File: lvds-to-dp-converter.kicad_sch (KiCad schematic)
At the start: 0 parts

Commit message: [#81876] Hierarchical design review fixes
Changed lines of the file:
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@@
 		(rev "1.0.0")
 	)
-	(hierarchical_label "PCIE_x4{PCIE}"
-		(shape bidirectional)
-		(at 123.19 99.06 0)
+	(hierarchical_label "DSI{DSI}"
+		(shape input)
+		(at 82.55 85.09 180)
 		(effects
 			(font
 				(size 1.27 1.27)
 			)
-			(justify left)
+			(justify right)
 		)
 	)
-	(hierarchical_label "PCIE_REFCLK{PCIeREFCLK}"
-		(shape input)
-		(at 123.19 105.41 0)
+	(hierarchical_label "DP{DP}"
+		(shape output)
+		(at 153.67 88.9 0)
 		(effects
 			(font

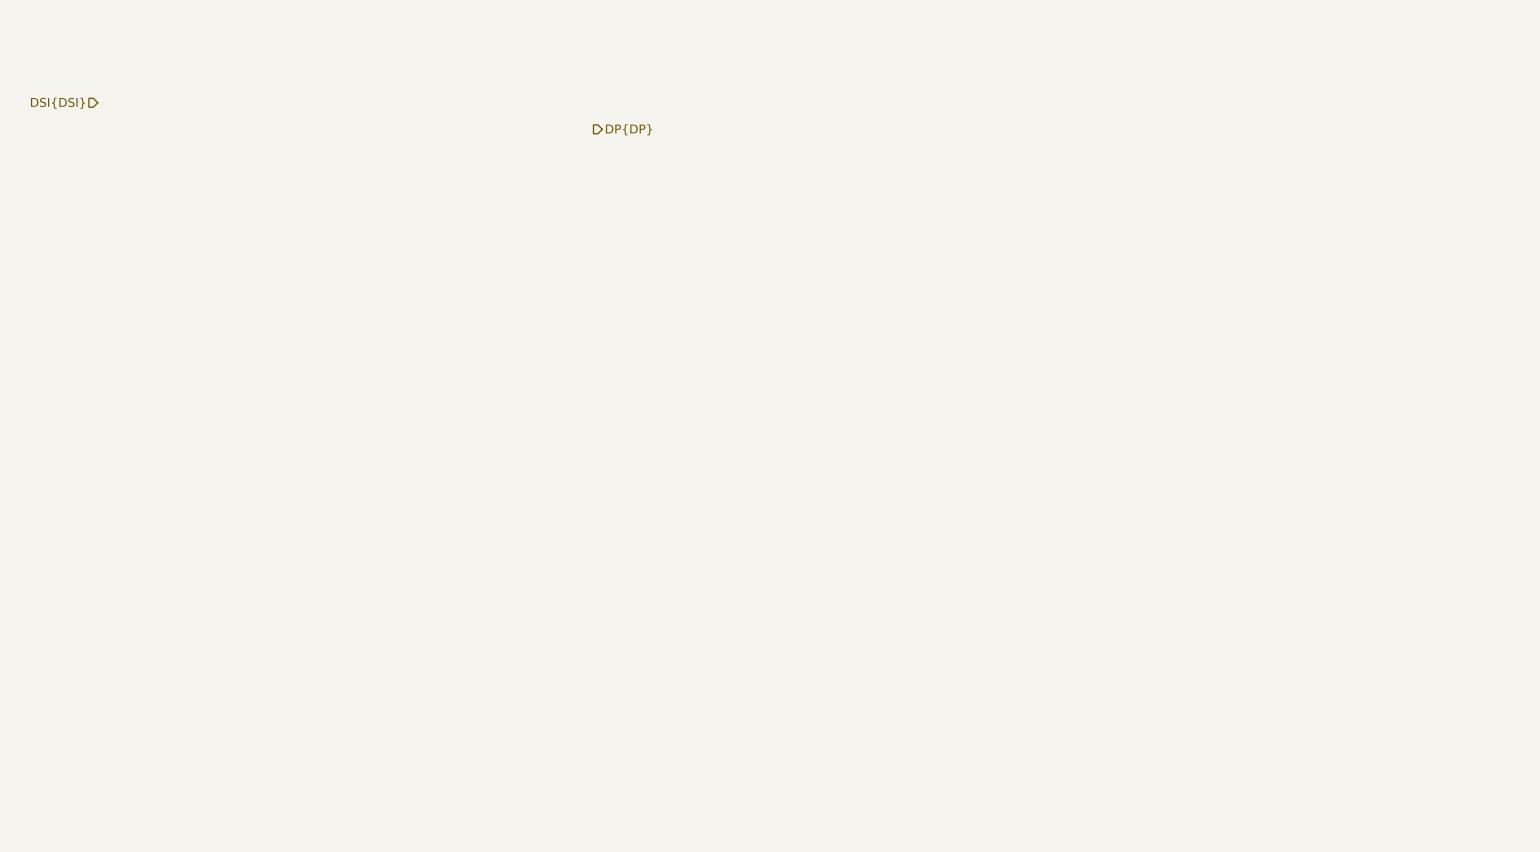
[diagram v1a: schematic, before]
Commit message: [#82341] LVDS/DP Bridge: Start placing pasive components
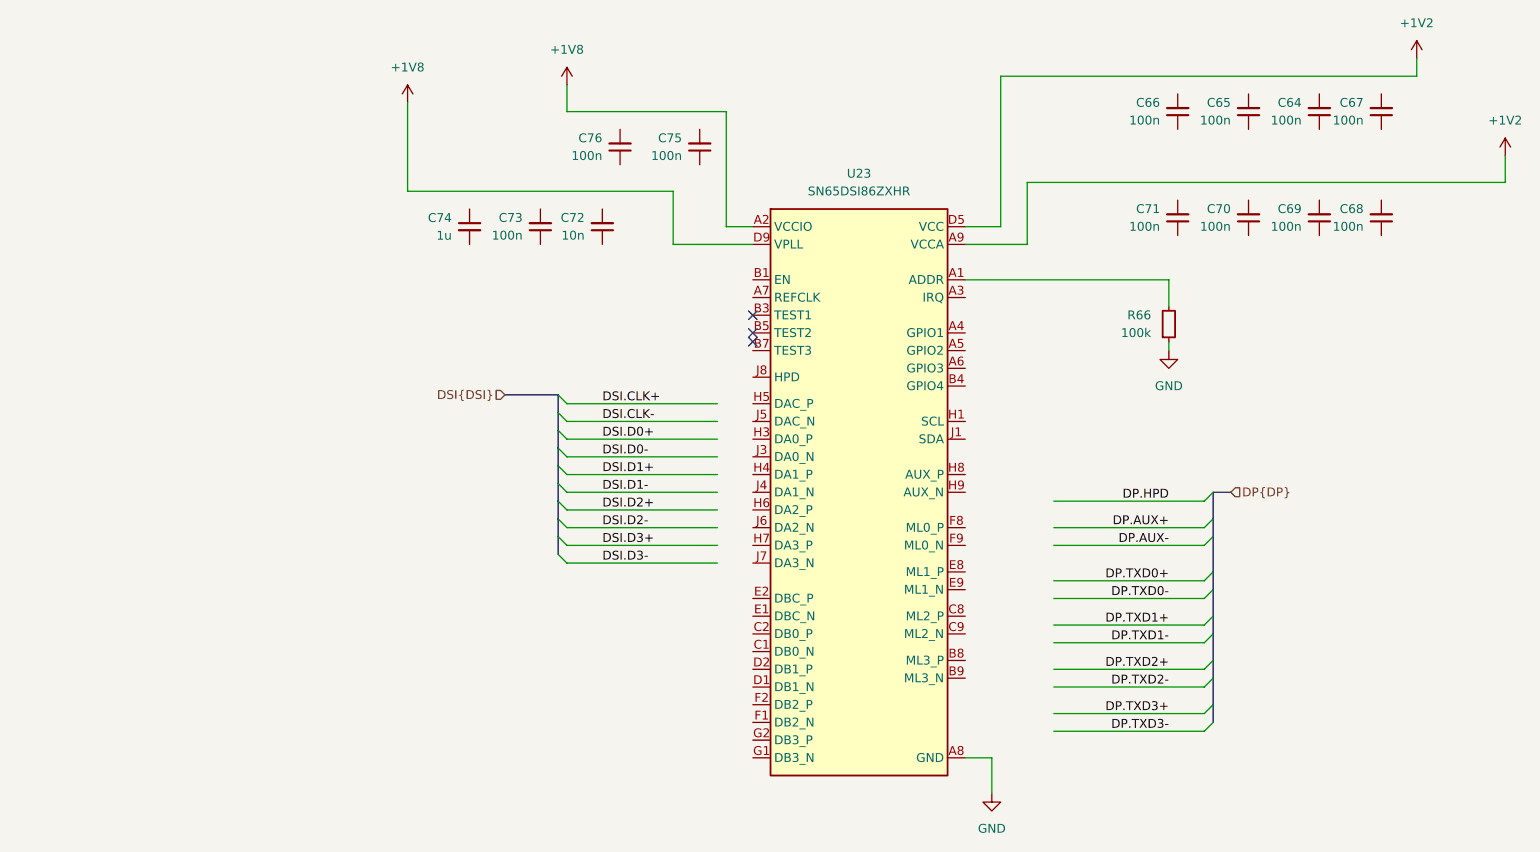
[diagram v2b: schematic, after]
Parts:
- added C64, C65, C66, C67, C68, C69, C70, C71, C73, C75, C76: C_100n_0402, antmicro-footprints:C_0402_1005Metric, symbol antmicroCapacitors0402:C_100n_0402
- added C72: C_10n_0402, antmicro-footprints:C_0402_1005Metric, symbol antmicroCapacitors0402:C_10n_0402
- added C74: C_1u_0402, antmicro-footprints:C_0402_1005Metric, symbol antmicroCapacitors0402:C_1u_0402
- added R66: R_100k_0402, antmicro-footprints:R_0402_1005Metric, symbol antmicroResistors0402:R_100k_0402
- added U23: SN65DSI86ZXHR, antmicro-footprints:NFBGA-64_5x5mm_Layout9X9_P0.5mm, symbol antmicroInterfaceControllers:SN65DSI86ZXHR
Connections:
- new net: R66.2, U23.A1 (ADDR)
- new net +1V2: U23.A9 (VCCA), U23.B2 (VCCA), U23.D5 (VCC), U23.D6 (VCC), U23.E6 (VCCA), U23.G9 (VCCA), U23.H2 (VCCA), U23.J2 (VCC), U23.J9 (VCC)
- new net +1V8: U23.A2 (VCCIO), U23.B6 (VCCIO), U23.D9 (VPLL)
- new net GND: R66.1, U23.A8 (GND), U23.D8 (GND), U23.E4 (GND), U23.E5 (GND), U23.F4 (GND), U23.F5 (GND), U23.F6 (GND), U23.G8 (GND)
- no-connect marks 0 -> 3

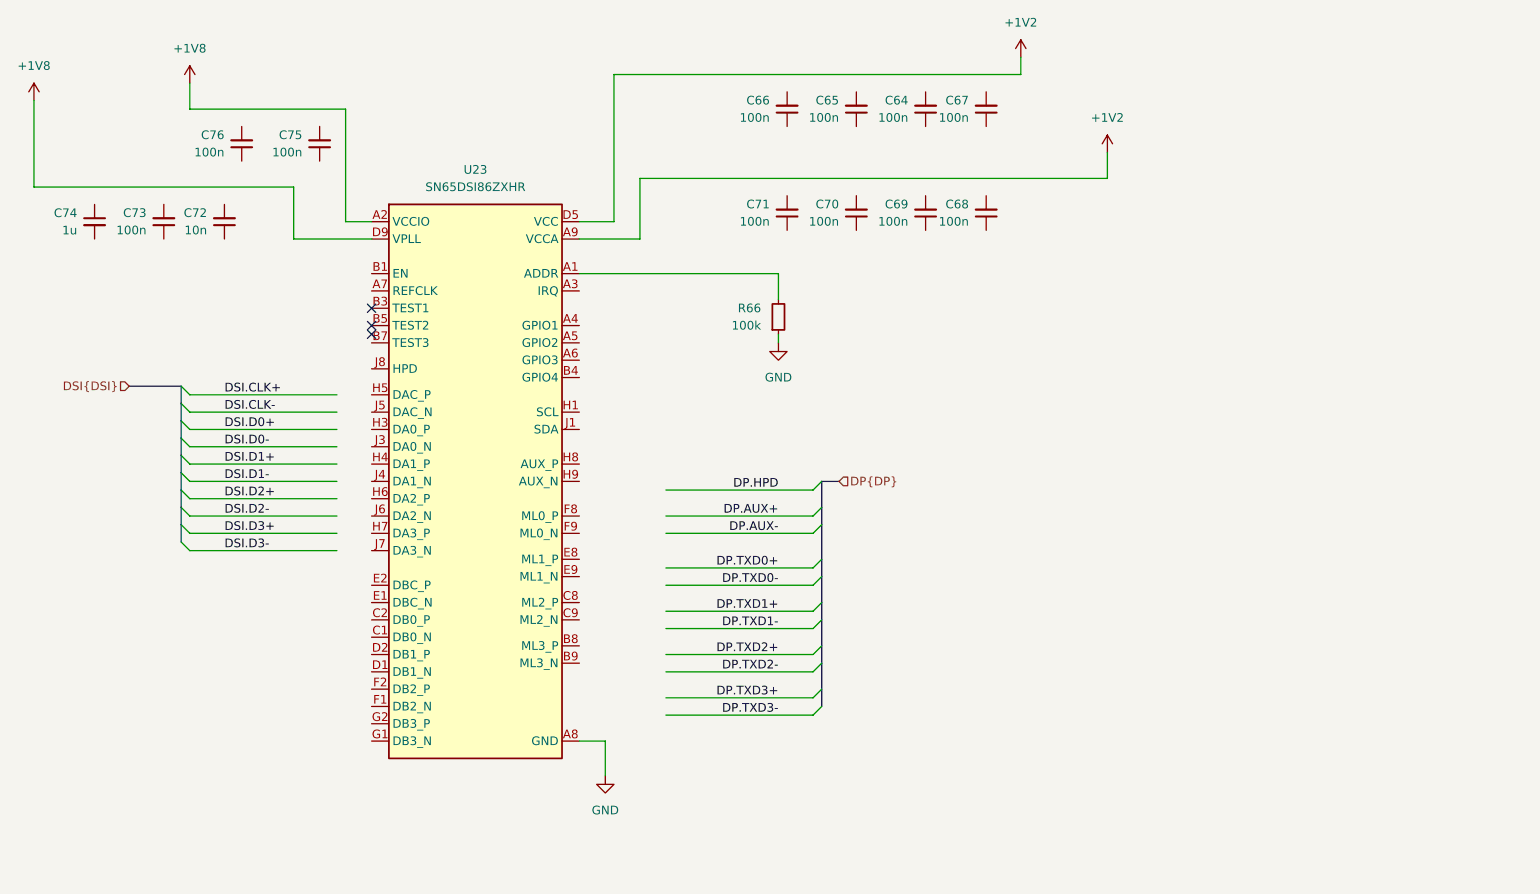
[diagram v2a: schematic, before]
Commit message: [#82341] LVDS/DP Bridge: Add 1V2 and 1V8 LDOs
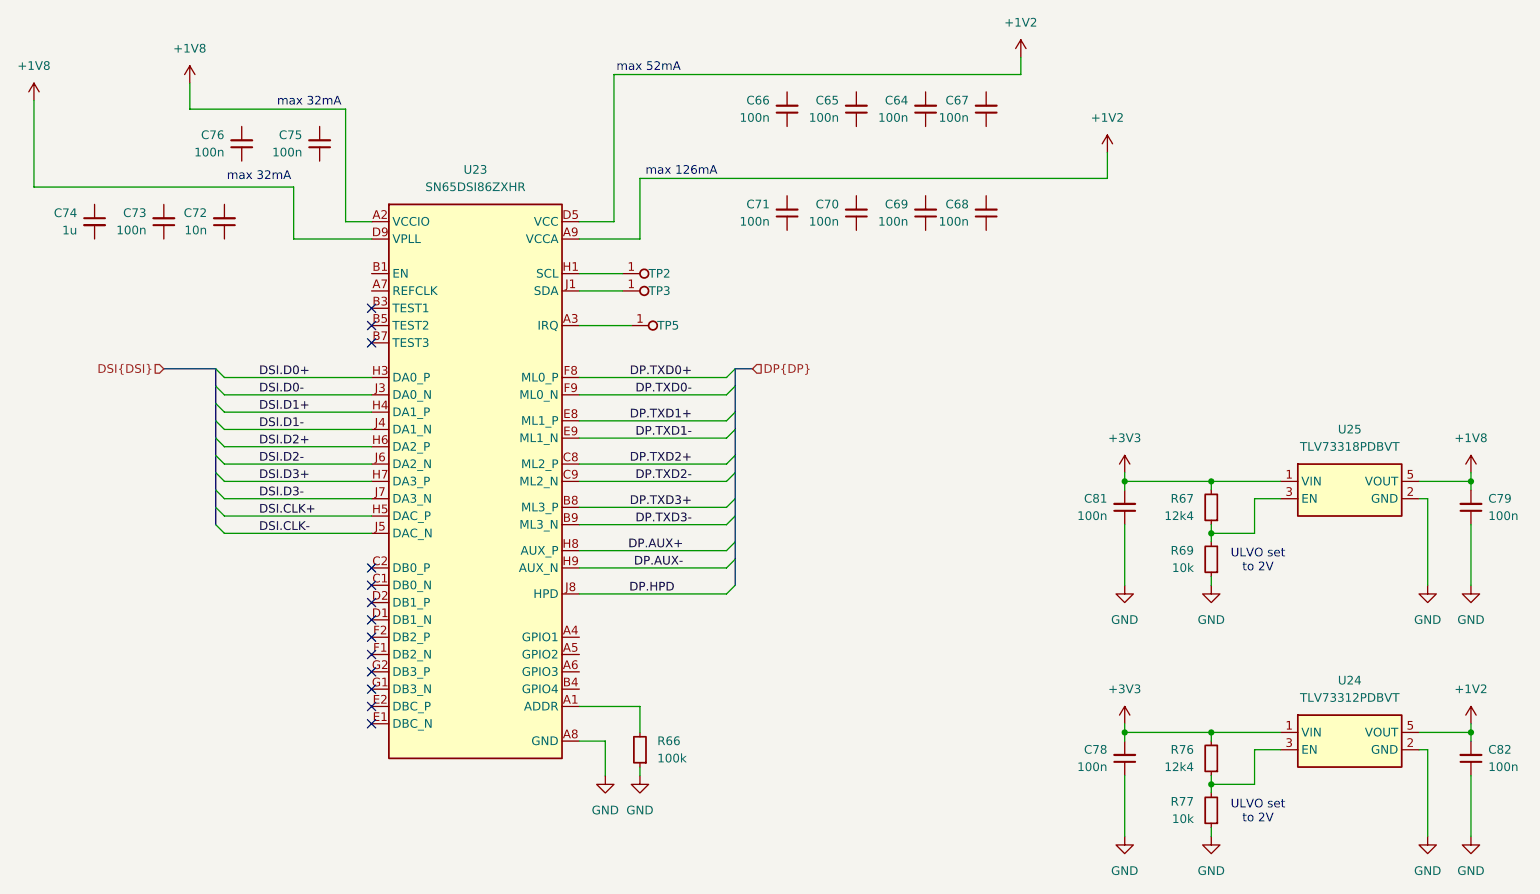
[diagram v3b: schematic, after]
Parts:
- added C78, C79, C81, C82: C_100n_0402, antmicro-footprints:C_0402_1005Metric, symbol antmicroCapacitors0402:C_100n_0402
- added R67, R76: R_12k4_0402, antmicro-footprints:R_0402_1005Metric, symbol antmicroResistors0402:R_12k4_0402
- added R69, R77: R_10k_0402, antmicro-footprints:R_0402_1005Metric, symbol antmicroResistors0402:R_10k_0402
- added TP2, TP3, TP5: TP_0.75mm_SMD, antmicro-footprints:TP_SMD_0.75mm, symbol antmicroTestPoints:TP_0.75mm_SMD
- added U24: TLV73312PDBVT, antmicro-footprints:SOT-23-5, symbol antmicroPMICVoltageRegulatorsLinear:TLV73312PDBVT
- added U25: TLV73318PDBVT, antmicro-footprints:SOT-23-5, symbol antmicroPMICVoltageRegulatorsLinear:TLV73318PDBVT
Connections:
- net +1V2: now also C82.2, U24.5 (VOUT)
- net +1V8: now also C79.2, U25.5 (VOUT)
- net DP.AUX+: now also U23.H8 (AUX_P)
- net DP.AUX-: now also U23.H9 (AUX_N)
- net DP.HPD: now also U23.J8 (HPD)
- net DP.TXD0+: now also U23.F8 (ML0_P)
- net DP.TXD0-: now also U23.F9 (ML0_N)
- net DP.TXD1+: now also U23.E8 (ML1_P)
- net DP.TXD1-: now also U23.E9 (ML1_N)
- net DP.TXD2+: now also U23.C8 (ML2_P)
- net DP.TXD2-: now also U23.C9 (ML2_N)
- net DP.TXD3+: now also U23.B8 (ML3_P)
- net DP.TXD3-: now also U23.B9 (ML3_N)
- net DSI.CLK+: now also U23.H5 (DAC_P)
- net DSI.CLK-: now also U23.J5 (DAC_N)
- net DSI.D0+: now also U23.H3 (DA0_P)
- net DSI.D0-: now also U23.J3 (DA0_N)
- net DSI.D1+: now also U23.H4 (DA1_P)
- net DSI.D1-: now also U23.J4 (DA1_N)
- net DSI.D2+: now also U23.H6 (DA2_P)
- net DSI.D2-: now also U23.J6 (DA2_N)
- net DSI.D3+: now also U23.H7 (DA3_P)
- net DSI.D3-: now also U23.J7 (DA3_N)
- net GND: now also C78.1, C79.1, C81.1, C82.1, R69.1, R77.1, U24.2 (GND), U25.2 (GND)
- net at U23.A3 (IRQ): now also TP5.1
- net at U23.H1 (SCL): now also TP2.1
- net at U23.J1 (SDA): now also TP3.1
- new net: R67.1, R69.2, U25.3 (EN)
- new net: R76.1, R77.2, U24.3 (EN)
- new net +3V3: C78.2, C81.2, R67.2, R76.2, U24.1 (VIN), U25.1 (VIN)
- no-connect marks 3 -> 13
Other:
- note added: "ULVO set to 2V"
- note added: "max 126mA"
- note added: "max 32mA"
- note added: "max 52mA"
- moved on the sheet: R66

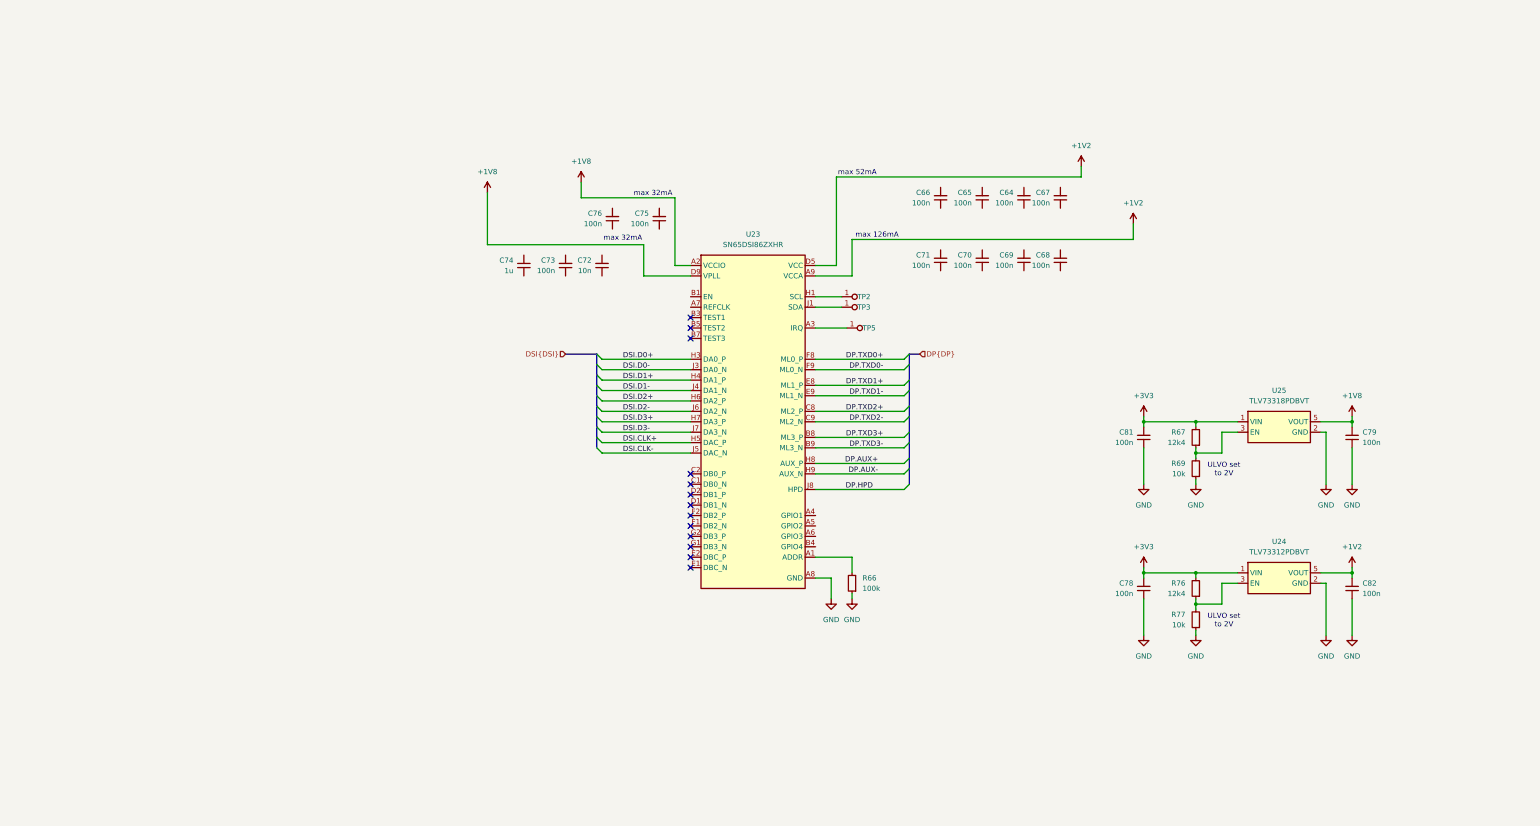
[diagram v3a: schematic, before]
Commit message: [#82341] LVDS/DP Bridge: Update power supply
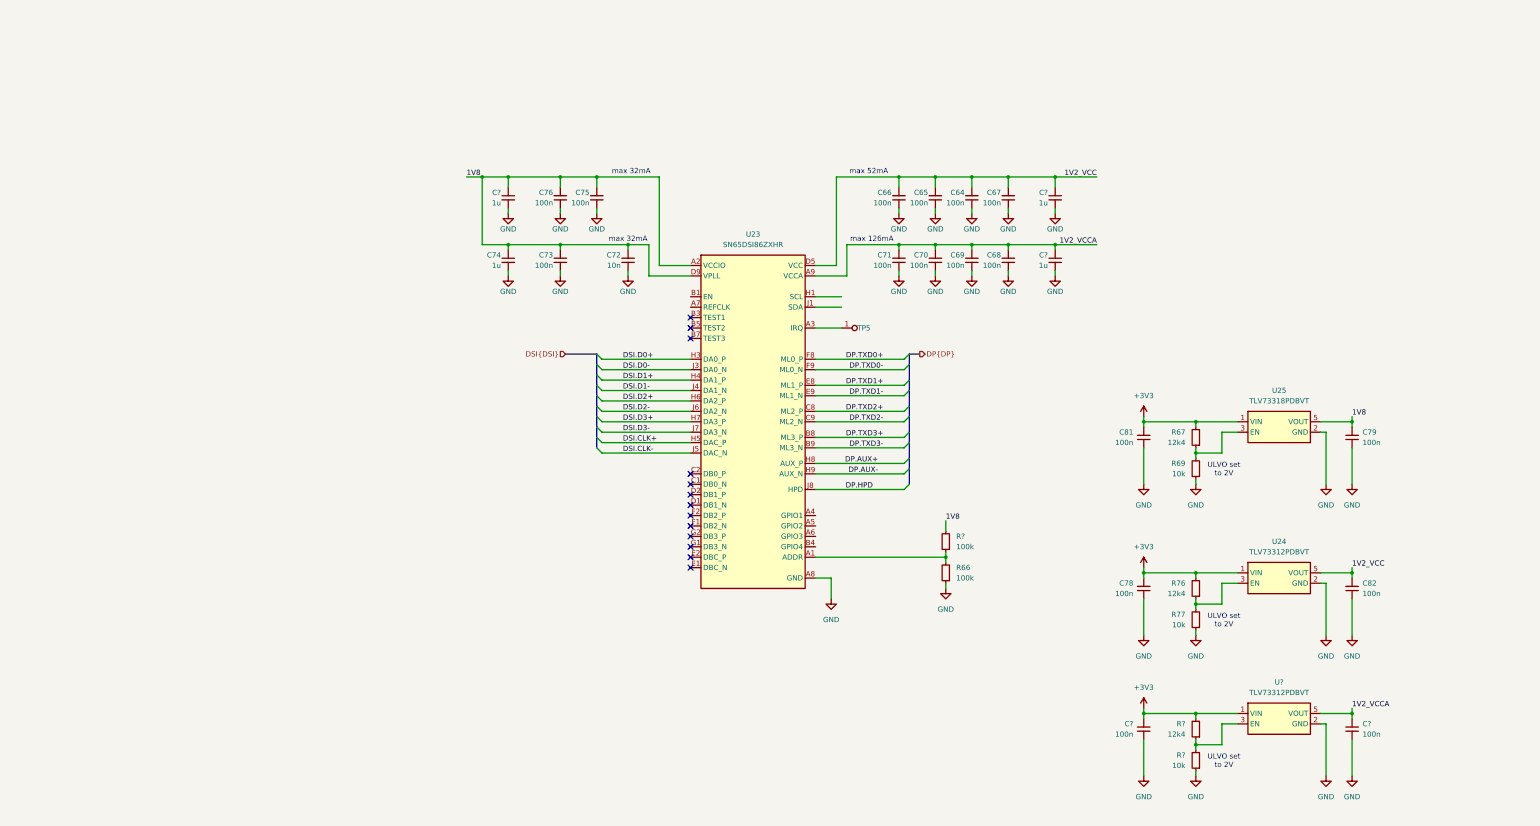
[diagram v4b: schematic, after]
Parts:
- removed TP2, TP3: TP_0.75mm_SMD, antmicro-footprints:TP_SMD_0.75mm, symbol antmicroTestPoints:TP_0.75mm_SMD
- added C? (x2): C_100n_0402, antmicro-footprints:C_0402_1005Metric, symbol antmicroCapacitors0402:C_100n_0402
- added C? (x3): C_1u_0402, antmicro-footprints:C_0402_1005Metric, symbol antmicroCapacitors0402:C_1u_0402
- added R?: R_100k_0402, antmicro-footprints:R_0402_1005Metric, symbol antmicroResistors0402:R_100k_0402
- added R?: R_12k4_0402, antmicro-footprints:R_0402_1005Metric, symbol antmicroResistors0402:R_12k4_0402
- added R?: R_10k_0402, antmicro-footprints:R_0402_1005Metric, symbol antmicroResistors0402:R_10k_0402
- added U?: TLV73312PDBVT, antmicro-footprints:SOT-23-5, symbol antmicroPMICVoltageRegulatorsLinear:TLV73312PDBVT
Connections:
- net +1V8 is gone; now on net VCCIO: C79.2, U23.A2 (VCCIO), U23.B6 (VCCIO), U23.D9 (VPLL), U25.5 (VOUT)
- net +3V3: now also C?.2, R?.2, U?.1 (VIN)
- net GND: now also C64.1, C65.1, C66.1, C67.1, C68.1, C69.1, C70.1, C71.1, C72.1, C73.1, C74.2, C75.1, C76.1, C?.1, C?.1, C?.2, C?.2, C?.2, R?.1, U?.2 (GND)
- net VCCIO: now reaches C72.2
- net VCCIO: now also C73.2, C74.1, C75.2, C76.2, C?.1, R?.2
- net VCCA: now reaches C71.2
- net VCCA: now also C68.2, C69.2, C70.2, U23.A9 (VCCA), U23.B2 (VCCA), U23.E6 (VCCA), U23.G9 (VCCA), U23.H2 (VCCA), C?.1, C?.2, U?.5 (VOUT)
- net VCC: now reaches C65.2
- net VCC: now also C64.2, C66.2, C67.2, C82.2, U23.D5 (VCC), U23.D6 (VCC), U23.J2 (VCC), U23.J9 (VCC), U24.5 (VOUT), C?.1
- net at R66.2, U23.A1 (ADDR): now also R?.1
- removed net +1V2: C82.2, U23.A9 (VCCA), U23.B2 (VCCA), U23.D5 (VCC), U23.D6 (VCC), U23.E6 (VCCA), U23.G9 (VCCA), U23.H2 (VCCA), U23.J2 (VCC), U23.J9 (VCC), U24.5 (VOUT)
- new net: R?.1, R?.2, U?.3 (EN)
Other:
- moved on the sheet: C64, C65, C66, C67, C68, C69, C70, C71, C72, C73, C74, C75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
